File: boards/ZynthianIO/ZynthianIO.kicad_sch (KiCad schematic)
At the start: 26 parts, among them J1 Btn-1, J1 Raspberry_Pi_2_3, J10 Ctrl-2, J11 Display, J3 Btn-2, J7 Ctrl-3, J8 Ctrl-4, J9 Ctrl-1, U1 MCP23017_SP, U2 6N138, U3 74LS14

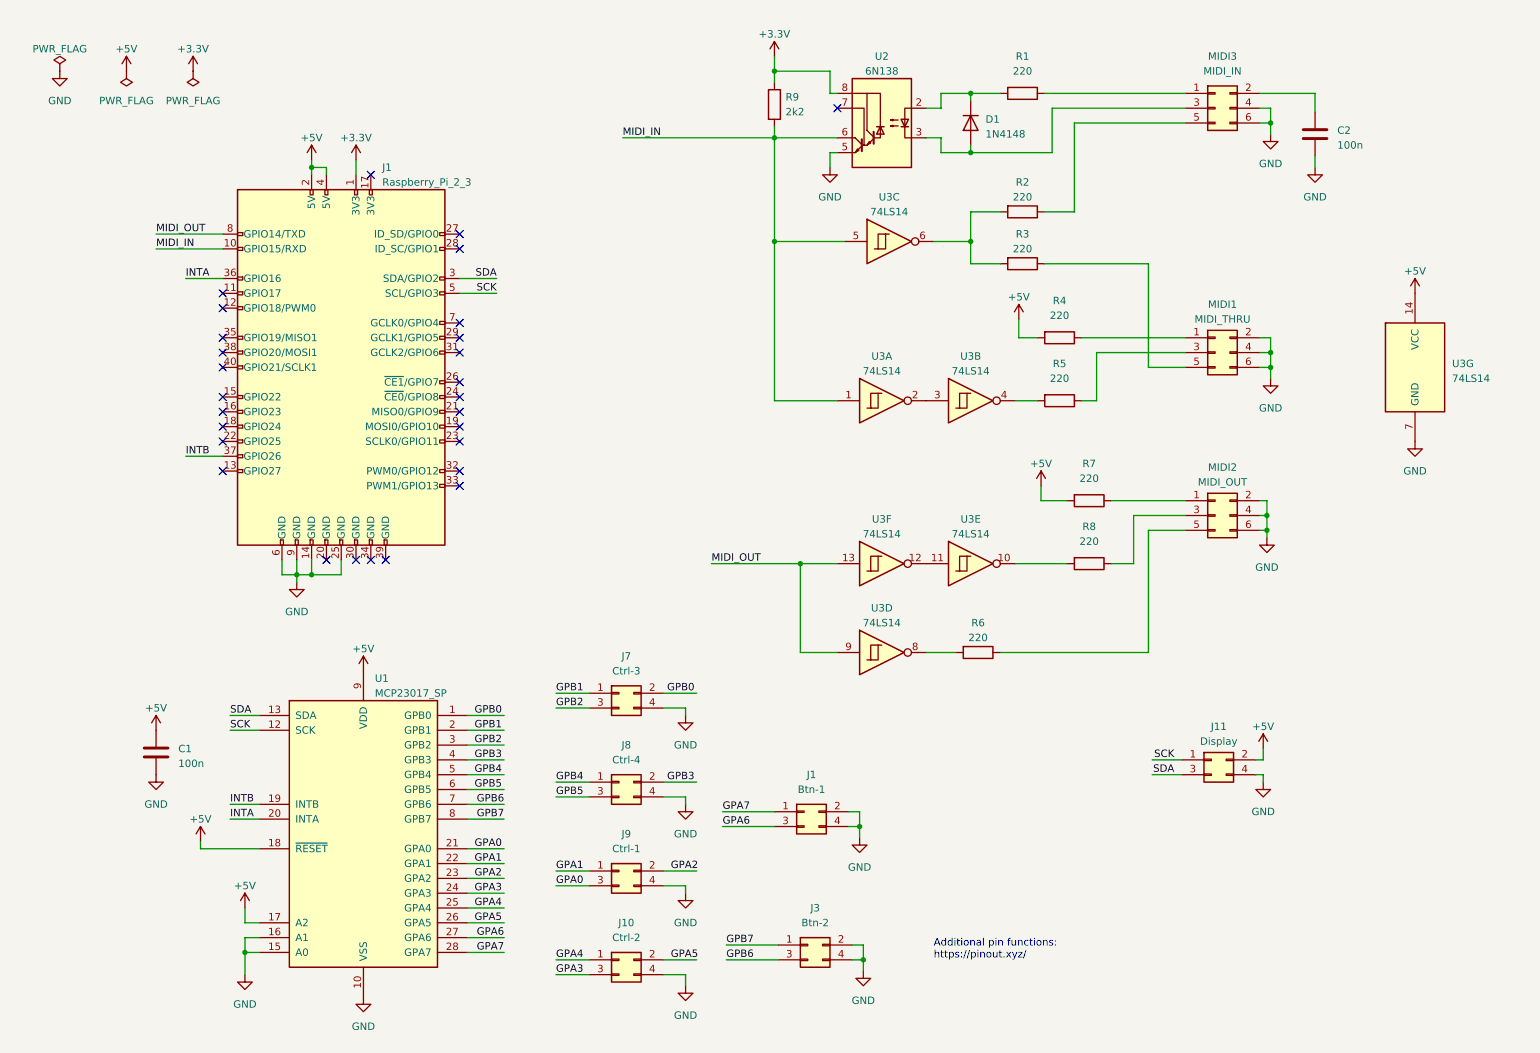
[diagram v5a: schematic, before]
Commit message: Updated to KiCAD 8, use H11L1 as optocoupler
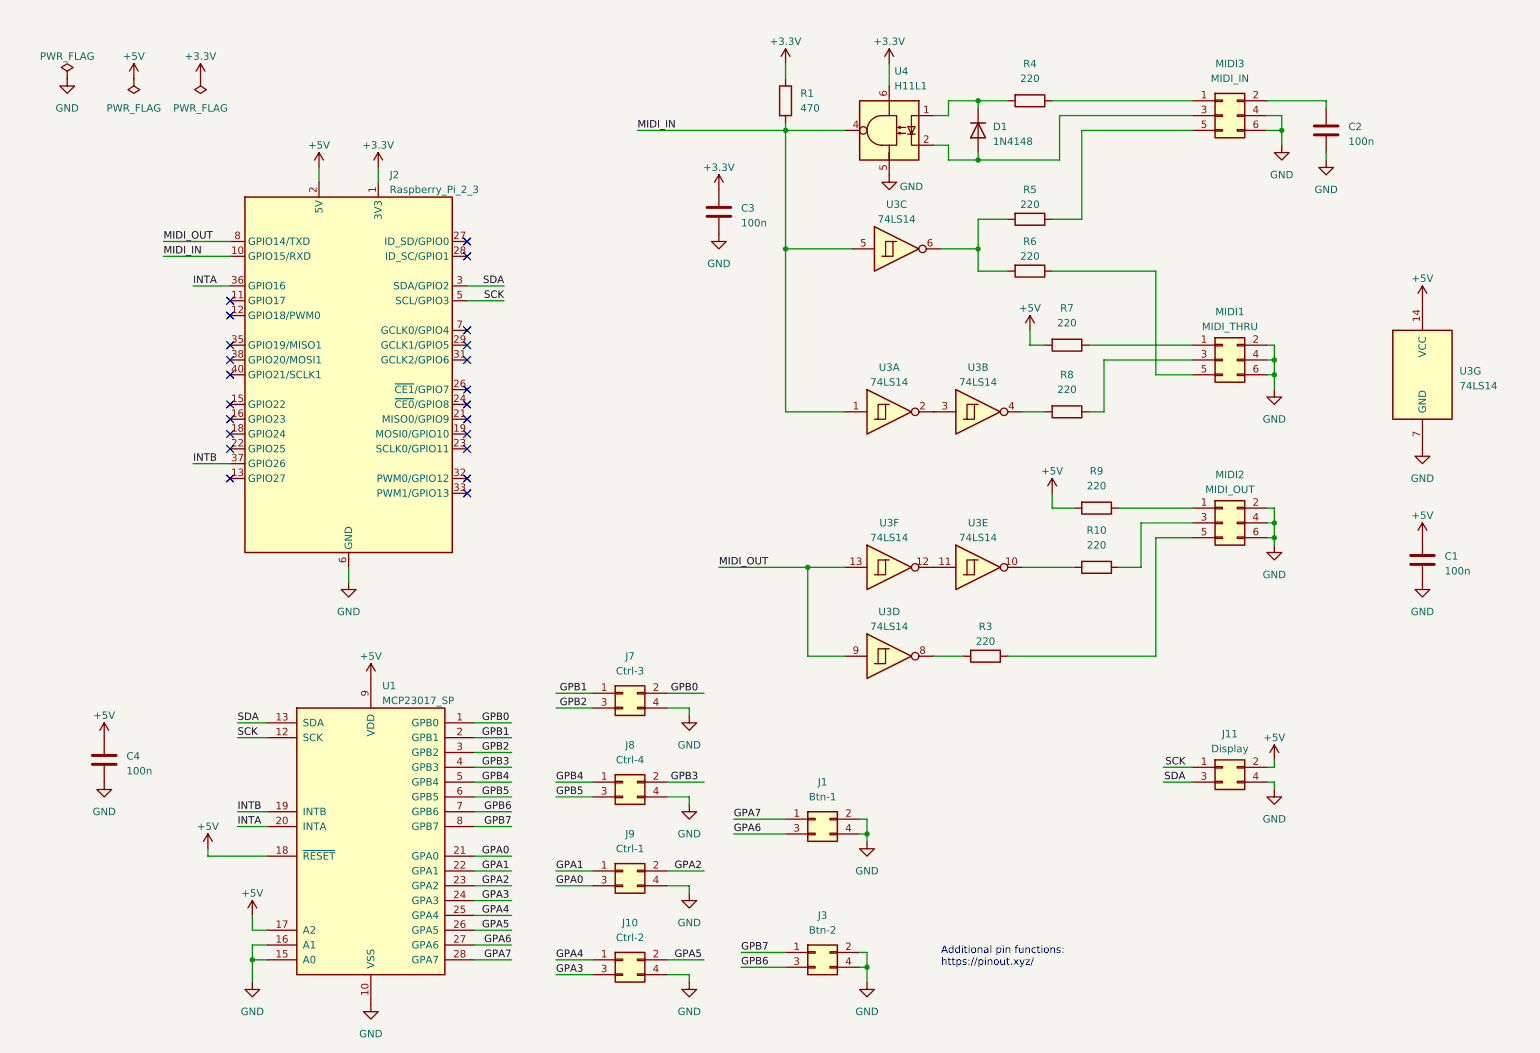
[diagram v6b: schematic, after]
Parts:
- removed U2: 6N138, Package_DIP:DIP-8_W7.62mm, symbol Isolator:6N138
- added C3, C4: 100n, Capacitor_THT:C_Disc_D5.0mm_W2.5mm_P5.00mm, symbol Device:C
- added U4: H11L1, Package_DIP:DIP-6_W7.62mm, symbol Isolator:H11L1
- R1: renamed from R9; value 2k2 -> 470
- renumbered J1 to J2, R8 to R10, R6 to R3, R1 to R4, R2 to R5, R3 to R6, R4 to R7, R5 to R8, R7 to R9
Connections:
- net +3.3V: now also J2.17 (3V3), C3.1, U4.6
- net +5V: now also C4.1
- net GND: now also J2.20 (GND), J2.30 (GND), J2.34 (GND), J2.39 (GND), C3.2, C4.2, U4.5
- net MIDI_IN: now also U4.4
- net at D1.1 (K), R4.2: now also U4.1
- net at D1.2 (A), MIDI3.3 (Pin_3): now also U4.2
- no-connect marks 28 -> 22
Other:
- moved on the sheet: C1, C2, D1, J1, J10, J11, J3, J7, J8, J9, MIDI1, MIDI2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

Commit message: Using 74LS07 OC buffer to avoid excessive LED currents
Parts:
- removed U3: 74LS14, Package_DIP:DIP-14_W7.62mm, symbol 74xx:74LS14
- added MH1, MH2, MH3, MH4: MountingHole, MountingHole:MountingHole_2.7mm_M2.5, symbol Mechanical:MountingHole
- added U2: 74LS07, Package_DIP:DIP-14_W7.62mm, symbol 74xx:74LS07
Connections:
- net +5V: now also MIDI1.6 (Pin_6), MIDI2.6 (Pin_6), MIDI3.6 (Pin_6), U2.13, U2.14 (VCC)
- net GND: now also U2.1, U2.7 (GND); no longer MIDI1.4 (Pin_4), MIDI1.6 (Pin_6), MIDI2.4 (Pin_4), MIDI2.6 (Pin_6), MIDI3.4 (Pin_4), MIDI3.6 (Pin_6)
- net MIDI_IN: now also U2.3, U2.5
- net MIDI_OUT: now also U2.11, U2.9
- net at R8.2: now also U2.4
- net at R5.2, R6.2: now also U2.6
- net at R10.2: now also U2.10
- net at R3.2: now also U2.8
- no-connect marks 22 -> 27
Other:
- moved on the sheet: C1, R3, R7, R8

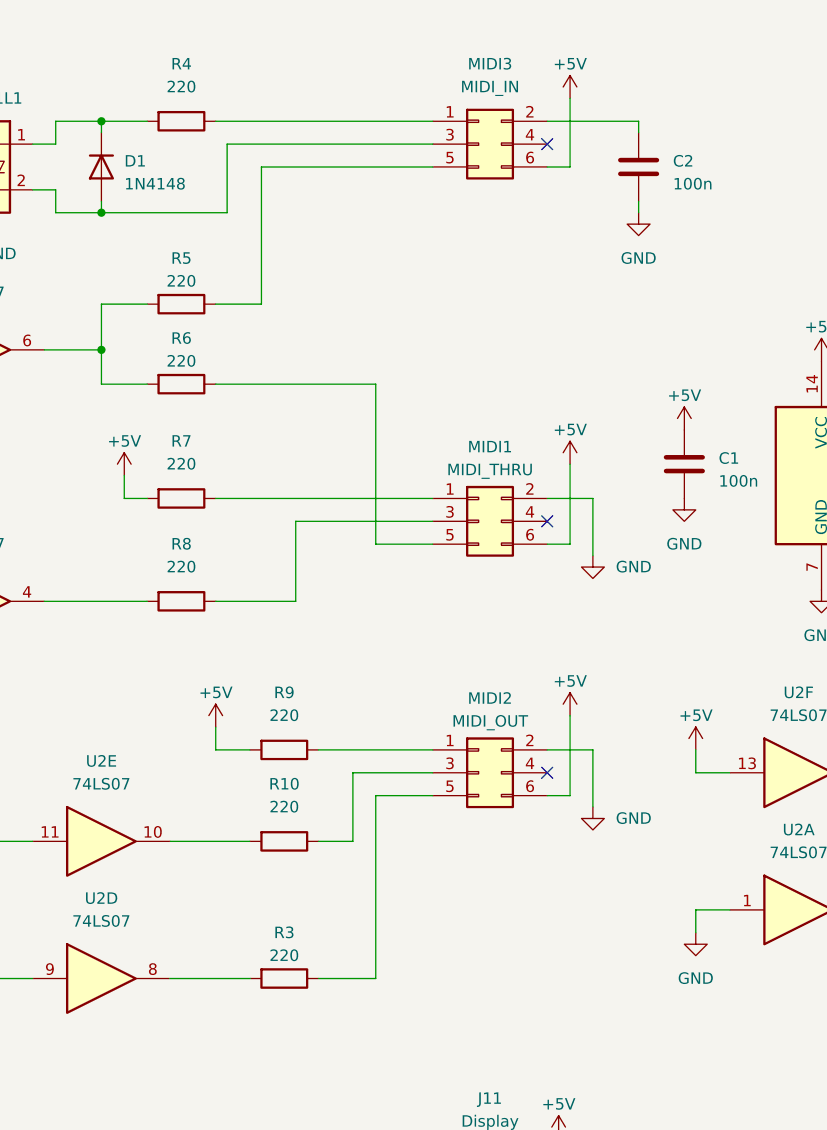
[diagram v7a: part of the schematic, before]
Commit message: Fixed resistor footprints and USB cutout locations
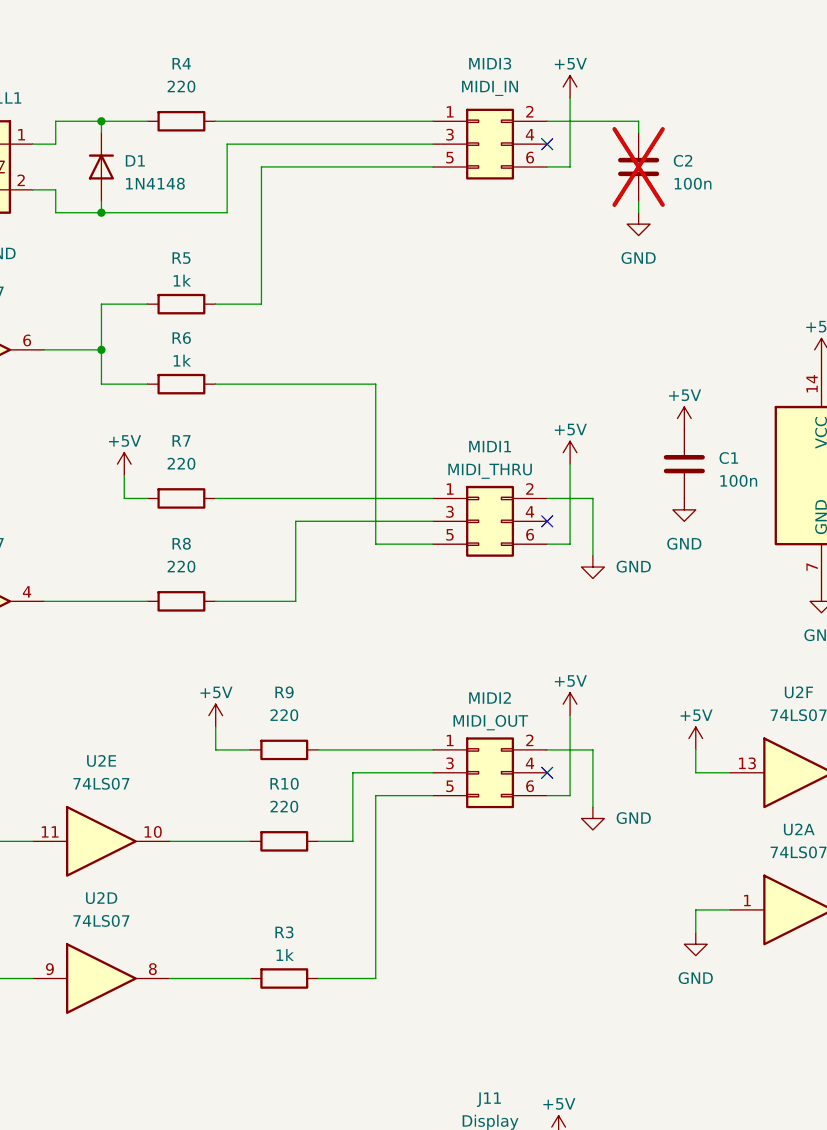
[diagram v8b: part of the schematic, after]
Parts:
- C2: now not fitted
- R1, R10, R4, R7, R8, R9: footprint Resistor_THT:R_Axial_DIN0207_L6.3mm_D2.5mm_P7.62mm_Horizontal -> Resistor_THT:R_Axial_DIN0207_L6.3mm_D2.5mm_P10.16mm_Horizontal
- R3, R5, R6: value 220 -> 1k; footprint Resistor_THT:R_Axial_DIN0207_L6.3mm_D2.5mm_P7.62mm_Horizontal -> Resistor_THT:R_Axial_DIN0207_L6.3mm_D2.5mm_P10.16mm_Horizontal
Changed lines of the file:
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@@
 			)
 		)
-		(property "Value" "220"
+		(property "Value" "1k"
 			(at 195.58 59.69 90)
 			(effects
@@
 			)
 		)
-		(property "Footprint" "Resistor_THT:R_Axial_DIN0207_L6.3mm_D2.5mm_P7.62mm_Horizontal"
+		(property "Footprint" "Resistor_THT:R_Axial_DIN0207_L6.3mm_D2.5mm_P10.16mm_Horizontal"
 			(at 195.58 60.452 90)
 			(effects
@@
 			)
 		)
-		(property "Footprint" "Resistor_THT:R_Axial_DIN0207_L6.3mm_D2.5mm_P7.62mm_Horizontal"
+		(property "Footprint" "Resistor_THT:R_Axial_DIN0207_L6.3mm_D2.5mm_P10.16mm_Horizontal"
 			(at 195.58 84.582 90)
 			(effects
@@
 			)
 		)
-		(property "Footprint" "Resistor_THT:R_Axial_DIN0207_L6.3mm_D2.5mm_P7.62mm_Horizontal"
+		(property "Footprint" "Resistor_THT:R_Axial_DIN0207_L6.3mm_D2.5mm_P10.16mm_Horizontal"
 			(at 207.01 101.092 90)
 			(effects
@@
 			)
 		)
-		(property "Footprint" "Resistor_THT:R_Axial_DIN0207_L6.3mm_D2.5mm_P7.62mm_Horizontal"
+		(property "Footprint" "Resistor_THT:R_Axial_DIN0207_L6.3mm_D2.5mm_P10.16mm_Horizontal"
 			(at 207.01 111.252 90)
 			(effects
@@
 			)
 		)
-		(property "Footprint" "Resistor_THT:R_Axial_DIN0207_L6.3mm_D2.5mm_P7.62mm_Horizontal"
+		(property "Footprint" "Resistor_THT:R_Axial_DIN0207_L6.3mm_D2.5mm_P10.16mm_Horizontal"
 			(at 195.58 31.242 90)
 			(effects
@@
 			)
 		)
-		(property "Footprint" "Resistor_THT:R_Axial_DIN0207_L6.3mm_D2.5mm_P7.62mm_Horizontal"
+		(property "Footprint" "Resistor_THT:R_Axial_DIN0207_L6.3mm_D2.5mm_P10.16mm_Horizontal"
 			(at 151.892 33.02 90)
 			(effects
@@
 			)
 		)
-		(property "Footprint" "Resistor_THT:R_Axial_DIN0207_L6.3mm_D2.5mm_P7.62mm_Horizontal"
+		(property "Footprint" "Resistor_THT:R_Axial_DIN0207_L6.3mm_D2.5mm_P10.16mm_Horizontal"
 			(at 195.58 73.152 90)
 			(effects
@@
 			)
 		)
-		(property "Value" "220"
+		(property "Value" "1k"
 			(at 195.58 50.8 90)
 			(effects
@@
 			)
 		)
-		(property "Footprint" "Resistor_THT:R_Axial_DIN0207_L6.3mm_D2.5mm_P7.62mm_Horizontal"
+		(property "Footprint" "Resistor_THT:R_Axial_DIN0207_L6.3mm_D2.5mm_P10.16mm_Horizontal"
 			(at 195.58 51.562 90)
 			(effects
@@
 			)
 		)
-		(property "Value" "220"
+		(property "Value" "1k"
 			(at 207.01 125.73 90)
 			(effects
@@
 			)
 		)
-		(property "Footprint" "Resistor_THT:R_Axial_DIN0207_L6.3mm_D2.5mm_P7.62mm_Horizontal"
+		(property "Footprint" "Resistor_THT:R_Axial_DIN0207_L6.3mm_D2.5mm_P10.16mm_Horizontal"
 			(at 207.01 126.492 90)
 			(effects
@@
 		(in_bom yes)
 		(on_board yes)
-		(dnp no)
+		(dnp yes)
 		(property "Reference" "C2"
 			(at 250.19 37.465 0)
